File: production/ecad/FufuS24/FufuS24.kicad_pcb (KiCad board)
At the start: 4 copper layers, 120 x 120 mm, 144 parts, among them J1 Conn_01x02, J10 691137710002, J11 USB_B_Micro, J12 691137710002, J13 5033950410, J2 Conn_01x02, J3 691137710002, J5 691137710004, J6 5025840270, J7 691137710002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

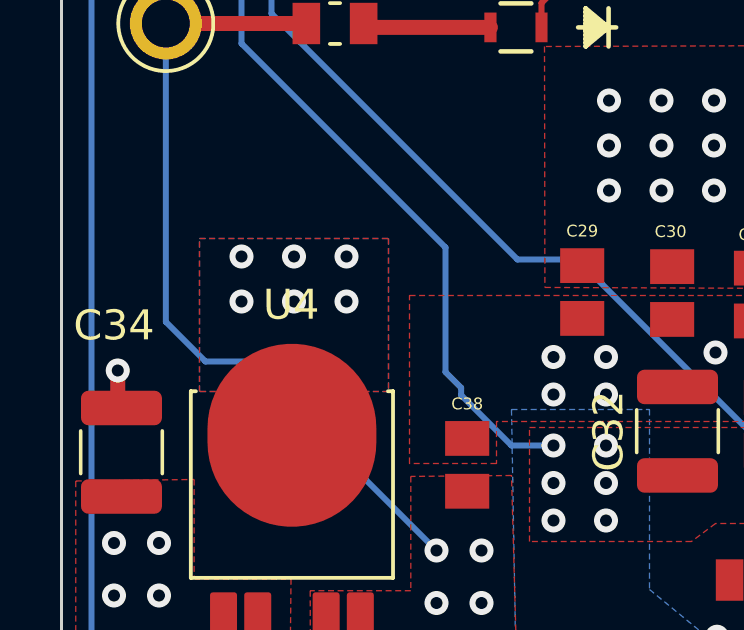
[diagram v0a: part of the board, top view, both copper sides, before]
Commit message: swapped layers
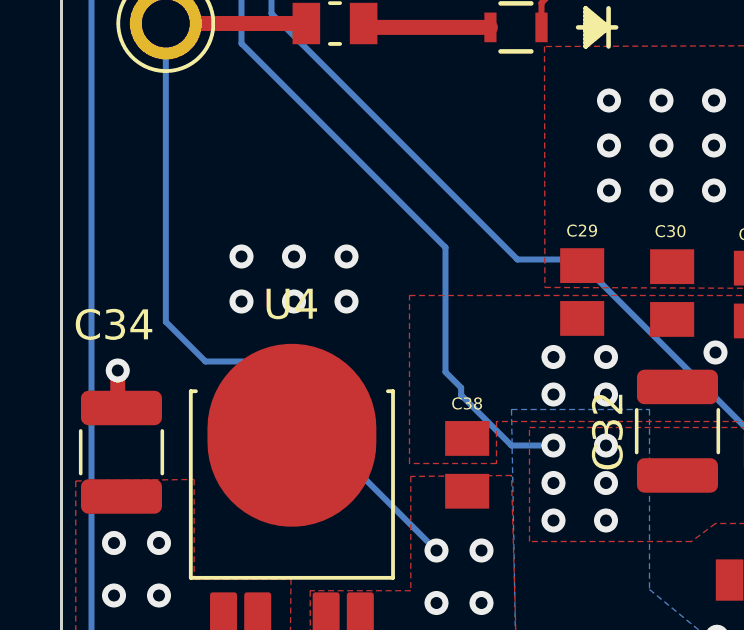
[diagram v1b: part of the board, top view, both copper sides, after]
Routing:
- added copper zone on In2.Cu, net +12V
- added copper zone on In2.Cu, net +3.3V
- added copper zone on In2.Cu, net +48V
- added copper zone on In2.Cu, net +5V
- added copper zone on In1.Cu, net GNDREF
- removed copper zone on In1.Cu, net +12V
- removed copper zone on In1.Cu, net +3.3V
- removed copper zone on In1.Cu, net +48V
- removed copper zone on In1.Cu, net +5V
- removed copper zone on In2.Cu, net GNDREF
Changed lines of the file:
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@@
   (via (at 155.8 127.65) (size 0.8) (drill 0.4) (layers "F.Cu" "B.Cu") (free) (net 10))
   (via (at 137.25 126.4) (size 0.8) (drill 0.4) (layers "F.Cu" "B.Cu") (free) (net 10))
-  (segment (start 176.75 96.5) (end 176.25 96) (width 0.5) (layer "In1.Cu") (net 10))
-  (segment (start 176.25 96) (end 174.2 96) (width 0.5) (layer "In1.Cu") (net 10))
+  (segment (start 176.75 96.5) (end 176.25 96) (width 0.5) (layer "In2.Cu") (net 10))
+  (segment (start 176.25 96) (end 174.2 96) (width 0.5) (layer "In2.Cu") (net 10))
   (segment (start 104.575 85.575) (end 103.5 84.5) (width 0.2) (layer "B.Cu") (net 10))
   (segment (start 136.575 39) (end 140.75 39) (width 0.2) (layer "B.Cu") (net 10))
@@
   (segment (start 184.045 125.295) (end 184.25 125.5) (width 0.1348) (layer "F.Cu") (net 65))
   (segment (start 180.5 125.295) (end 184.045 125.295) (width 0.5) (layer "F.Cu") (net 65))
-  (segment (start 177.46 132.29) (end 184.25 125.5) (width 0.2) (layer "In2.Cu") (net 65))
-  (segment (start 175.06 132.29) (end 177.46 132.29) (width 0.2) (layer "In2.Cu") (net 65))
+  (segment (start 177.46 132.29) (end 184.25 125.5) (width 0.2) (layer "In1.Cu") (net 65))
+  (segment (start 175.06 132.29) (end 177.46 132.29) (width 0.2) (layer "In1.Cu") (net 65))
   (segment (start 120.0702 124.1694) (end 118.2668 125.9728) (width 0.5) (layer "F.Cu") (net 66))
   (segment (start 121.819149 124.1694) (end 120.0702 124.1694) (width 0.5) (layer "F.Cu") (net 66))
@@
     )
   )
-  (zone (net 2) (net_name "GNDREF") (layers "F&B.Cu") (hatch edge 0.5)
+  (zone (net 2) (net_name "GNDREF") (layer "In1.Cu") (hatch edge 0.5)
     (priority 15)
     (connect_pads yes (clearance 0.5))
@@
     )
   )
-  (zone (net 10) (net_name "+5V") (layer "In1.Cu") (hatch edge 0.5)
+  (zone (net 2) (net_name "GNDREF") (layer "In1.Cu") (hatch edge 0.5)
+    (priority 8)
+    (connect_pads yes (clearance 0.5))
+    (min_thickness 0.25) (filled_areas_thickness no)
+    (fill yes (thermal_gap 0.5) (thermal_bridge_width 0.5))
+    (polygon
+      (pts
+        (xy 75.725 23.175)
+        (xy 74.45 156.6)
+        (xy 210.775 157.15)
+        (xy 212.2 23.9)
+      )
+    )
+  )
+  (zone (net 10) (net_name "+5V") (layer "In2.Cu") (hatch edge 0.5)
     (priority 23)
     (connect_pads (clearance 0.5))
@@
     )
   )
-  (zone (net 10) (net_name "+5V") (layer "In1.Cu") (hatch edge 0.5)
+  (zone (net 10) (net_name "+5V") (layer "In2.Cu") (hatch edge 0.5)
     (priority 24)
     (connect_pads (clearance 0.5))
@@
     )
   )
-  (zone (net 10) (net_name "+5V") (layer "In1.Cu") (hatch edge 0.5)
+  (zone (net 10) (net_name "+5V") (layer "In2.Cu") (hatch edge 0.5)
     (priority 25)
     (connect_pads (clearance 0.5))
@@
     )
   )
-  (zone (net 10) (net_name "+5V") (layer "In1.Cu") (hatch edge 0.5)
+  (zone (net 10) (net_name "+5V") (layer "In2.Cu") (hatch edge 0.5)
     (priority 5)
     (connect_pads (clearance 0.5))
@@
     )
   )
-  (zone (net 10) (net_name "+5V") (layer "In1.Cu") (hatch edge 0.5)
+  (zone (net 10) (net_name "+5V") (layer "In2.Cu") (hatch edge 0.5)
     (priority 28)
     (connect_pads (clearance 0.5))
@@
     )
   )
-  (zone (net 1) (net_name "+48V") (layer "In1.Cu") (hatch edge 0.5)
+  (zone (net 1) (net_name "+48V") (layer "In2.Cu") (hatch edge 0.5)
     (priority 27)
     (connect_pads (clearance 0.5))
@@
     )
   )
-  (zone (net 15) (net_name "+12V") (layer "In1.Cu") (hatch edge 0.5)
+  (zone (net 15) (net_name "+12V") (layer "In2.Cu") (hatch edge 0.5)
     (priority 33)
     (connect_pads (clearance 0.5))
@@
     )
   )
-  (zone (net 1) (net_name "+48V") (layer "In1.Cu") (hatch edge 0.5)
+  (zone (net 1) (net_name "+48V") (layer "In2.Cu") (hatch edge 0.5)
     (priority 2)
     (connect_pads (clearance 0.5))
@@
     )
   )
-  (zone (net 15) (net_name "+12V") (layer "In1.Cu") (hatch edge 0.5)
+  (zone (net 15) (net_name "+12V") (layer "In2.Cu") (hatch edge 0.5)
     (priority 34)
     (connect_pads (clearance 0.45))
@@
     )
   )
-  (zone (net 19) (net_name "+3.3V") (layer "In1.Cu") (hatch edge 0.5)
+  (zone (net 19) (net_name "+3.3V") (layer "In2.Cu") (hatch edge 0.5)
     (priority 22)
     (connect_pads (clearance 0.5))
@@
       )
     )
-  )
-  (zone (net 2) (net_name "GNDREF") (layer "In2.Cu") (hatch edge 0.5)
-    (priority 8)
-    (connect_pads yes (clearance 0.5))
-    (min_thickness 0.25) (filled_areas_thickness no)
-    (fill yes (thermal_gap 0.5) (thermal_bridge_width 0.5))
-    (polygon
-      (pts
-        (xy 75.725 23.175)
-        (xy 74.45 156.6)
-        (xy 210.775 157.15)
-        (xy 212.2 23.9)
-      )
-    )

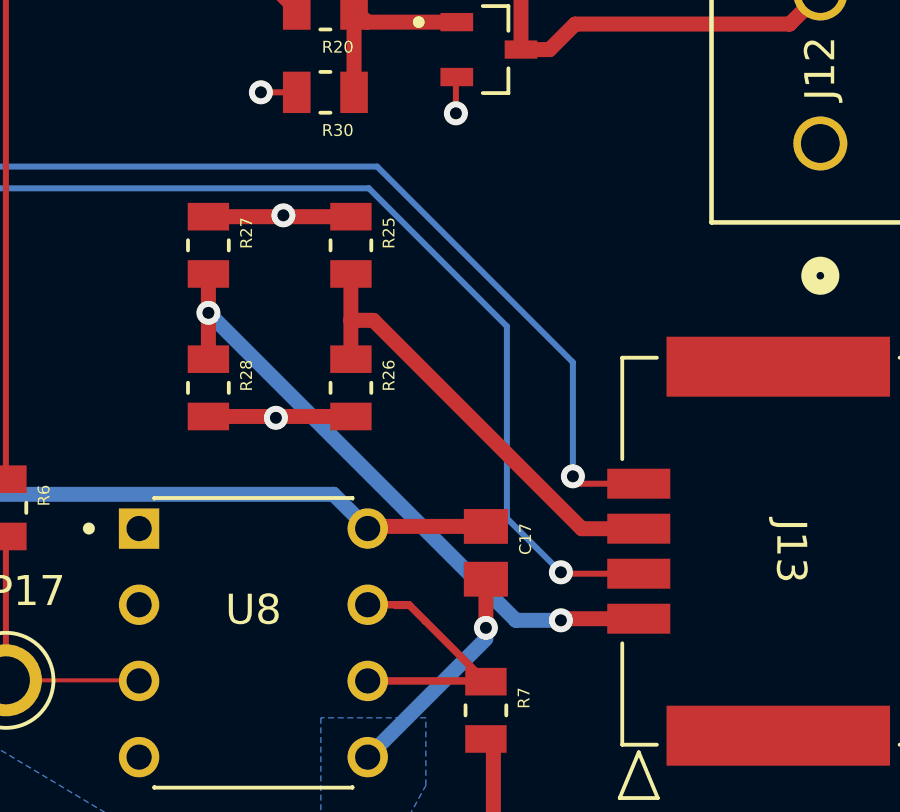
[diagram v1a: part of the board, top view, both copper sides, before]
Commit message: updated water sensor
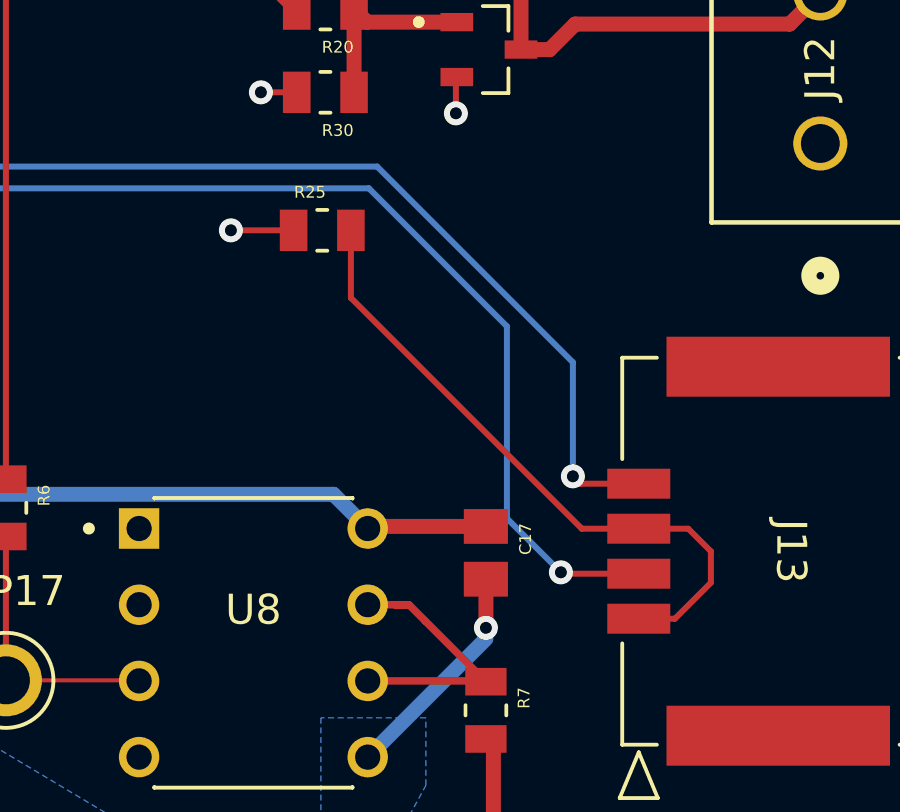
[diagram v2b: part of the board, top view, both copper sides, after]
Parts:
- removed R26, R27, R28: 10k, footprints:RESC2012X60N
- moved R25 1.08 mm to (178.0, 97.0), turned to 0 degrees
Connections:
- J13 pad 1: /Water Dispensing/Watersense_Mode_2 -> Net-(J13-Pad1)
- J13 pad 3: /Water Dispensing/Watersense_Mode_1 -> Net-(J13-Pad1)
- R25 pad 2: /Water Dispensing/Watersense_Mode_1 -> Net-(J13-Pad1)
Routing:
- net Net-(J13-Pad1): track 0.00 -> 21.7 mm
- net /Water Dispensing/Watersense_Mode_2: track 21.5 -> 0.00 mm, vias 2 -> 0
- net /Water Dispensing/Watersense_Mode_1: track 15.3 -> 0.00 mm
- net +5V: track 53.4 -> 48.0 mm
- net GNDREF: track 71.5 -> 66.7 mm, vias 93 -> 92

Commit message: updated layout
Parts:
- removed D10, D11: 150080GS75000, footprints:LED_GS75000_WRE
- removed R44, R45, R46: R_US, footprints:RESC2012X60N
- removed TP6, TP7, TP8: 5014, footprints:TP_5014
- removed U12: Pololu_DRV8711_Motor_Driver, footprints:POLOLU_36v4
- added C40: 100n, footprints:WCAP-CSGP_885012206026, F.Cu at (155.6, 50.3)
- added C41: 100n, footprints:WCAP-CSGP_885012206026, F.Cu at (162.0, 50.6)
- added J17: Conn_01x14_Socket, Connector_PinSocket_2.54mm:PinSocket_1x14_P2.54mm_Vertical, F.Cu at (194.9, 48.0)
- added R26: TBD, footprints:RESC2012X60N, F.Cu at (153.8, 50.4)
- added U3: TXS0101DBVR, footprints:LevelShifter_Motor, F.Cu at (158.8, 51.0)
- moved J2 54.2 mm to (156.2, 38.7), turned to 0 degrees
- moved R1 48.7 mm to (156.2, 42.6), turned to -90 degrees
- moved TP19 9.52 mm to (187.3, 44.8)
- moved J12 1.80 mm to (194.5, 95.9)
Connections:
- J5 pad 1: Net-(U12-BOUT2) -> GNDREF
- J5 pad 2: Net-(U12-BOUT1) -> unconnected-(J5-Pad2)
- J5 pad 3: Net-(U12-AOUT2) -> unconnected-(J5-Pad3)
- U1 pad 2: unconnected-(U1-GPIO0-Pad2) -> GPIO_0
- U1 pad 27: Motor_SLP -> GPIO_7
- U1 pad 28: Motor_RST -> GPIO_8
- U1 pad 3: unconnected-(U1-GPIO1-Pad3) -> GPIO_1
- U1 pad 30: unconnected-(U1-GPIO19-Pad30) -> GPIO_19
- U1 pad 36: Motor_SPI1_RX -> GPIO_24
- U1 pad 37: Motor_SPI1_CSn -> GPIO_25
- U1 pad 38: Motor_SPI1_CLK -> GPIO_26
- U1 pad 39: Motor_SPI1_TX -> GPIO_27
- U1 pad 5: unconnected-(U1-GPIO3-Pad5) -> GPIO_3
- U1 pad 6: Motor_BIN1 -> Motor_PWM
- U1 pad 7: Motor_BIN2 -> GPIO_4
- U1 pad 8: Motor_Step -> GPIO_5
- U1 pad 9: Motor_DIR -> GPIO_6
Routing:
- net Motor_RST: track 82.7 -> 0.00 mm, vias 1 -> 0
- net GPIO_5: track 0.00 -> 82.6 mm, vias 0 -> 1
- net GPIO_6: track 0.00 -> 82.3 mm, vias 0 -> 1
- net GPIO_4: track 0.00 -> 82.3 mm, vias 0 -> 1
- net GPIO_8: track 0.00 -> 81.9 mm, vias 0 -> 1
- net GPIO_7: track 0.00 -> 81.9 mm, vias 0 -> 1
- net GPIO_19: track 0.00 -> 81.4 mm, vias 0 -> 1
- net GPIO_3: track 0.00 -> 81.2 mm, vias 0 -> 1
- net GPIO_1: track 0.00 -> 81.1 mm, vias 0 -> 1
- net GPIO_0: track 0.00 -> 80.8 mm, vias 0 -> 1
- net GPIO_27: track 0.00 -> 80.2 mm, vias 0 -> 1
- net GPIO_26: track 0.00 -> 79.1 mm, vias 0 -> 1
- net GPIO_25: track 0.00 -> 78.1 mm, vias 0 -> 1
- net GPIO_24: track 0.00 -> 77.4 mm, vias 0 -> 1
- net Motor_SLP: track 76.6 -> 0.00 mm, vias 1 -> 0
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- removed copper zone on In2.Cu, net +12V
- removed copper zone on B.Cu, net +5V

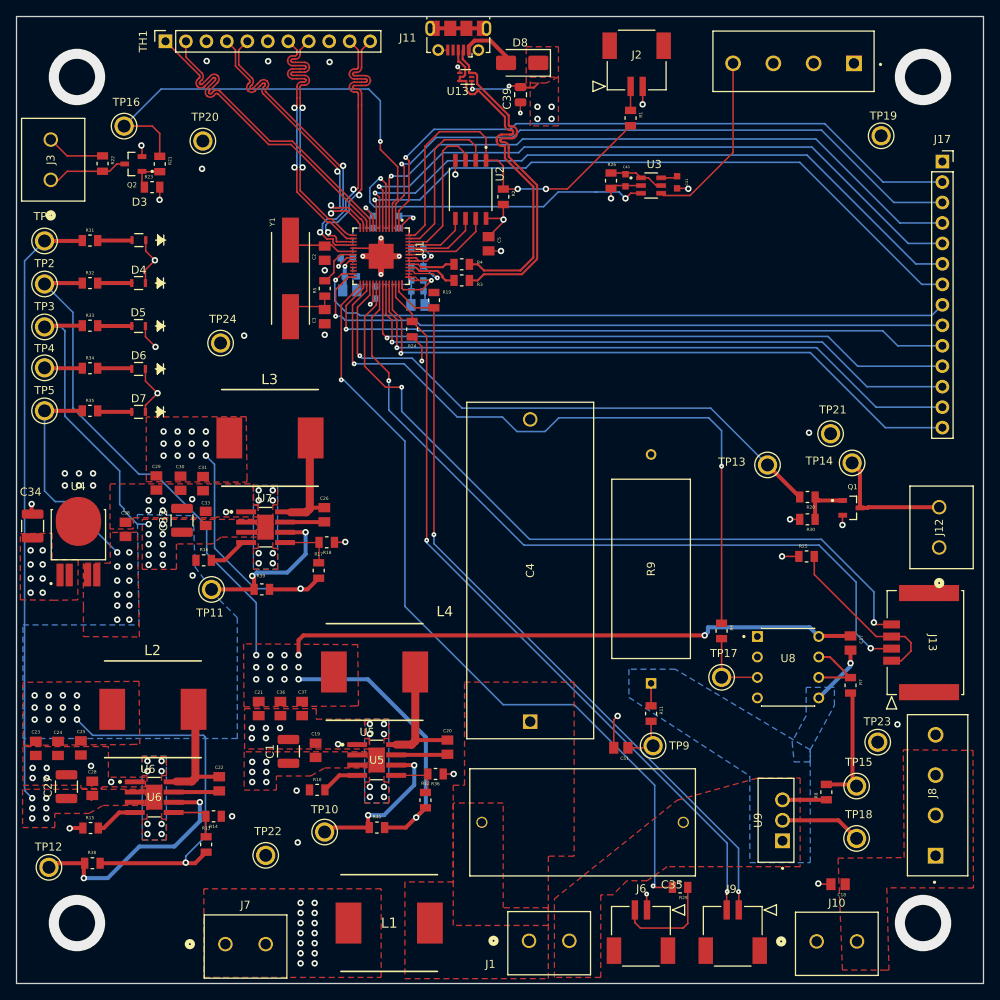
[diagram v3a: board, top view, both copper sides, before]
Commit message: updated power planes
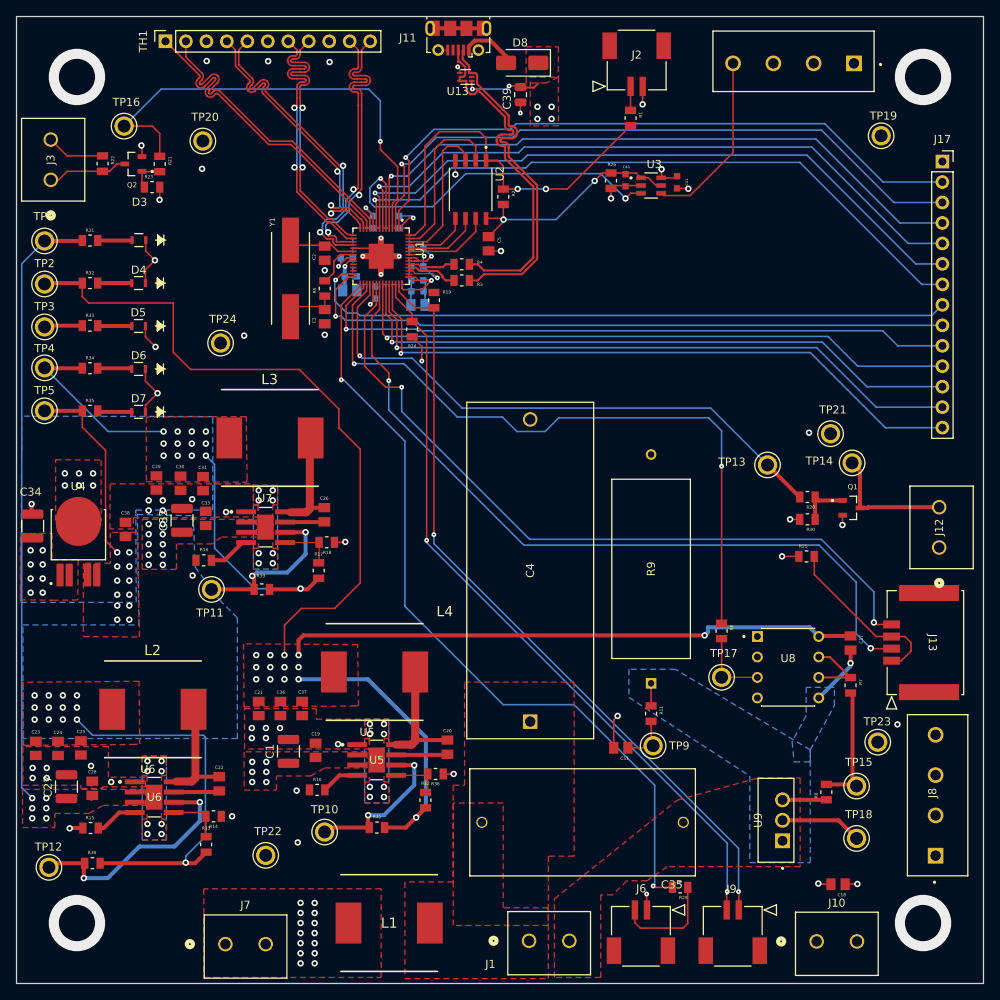
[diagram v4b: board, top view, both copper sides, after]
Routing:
- net +12V: track 91.2 -> 59.4 mm
- net +16V: track 169.4 -> 192.2 mm
- net +5V: track 50.0 -> 70.7 mm, vias 28 -> 30
- net +3.3V: track 83.2 -> 96.2 mm, vias 20 -> 21
- net Motor_PWM: track 45.6 -> 47.2 mm
- added copper zone on In2.Cu, net +12V
- added copper zone on B.Cu, net +5V

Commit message: fixed some DRC
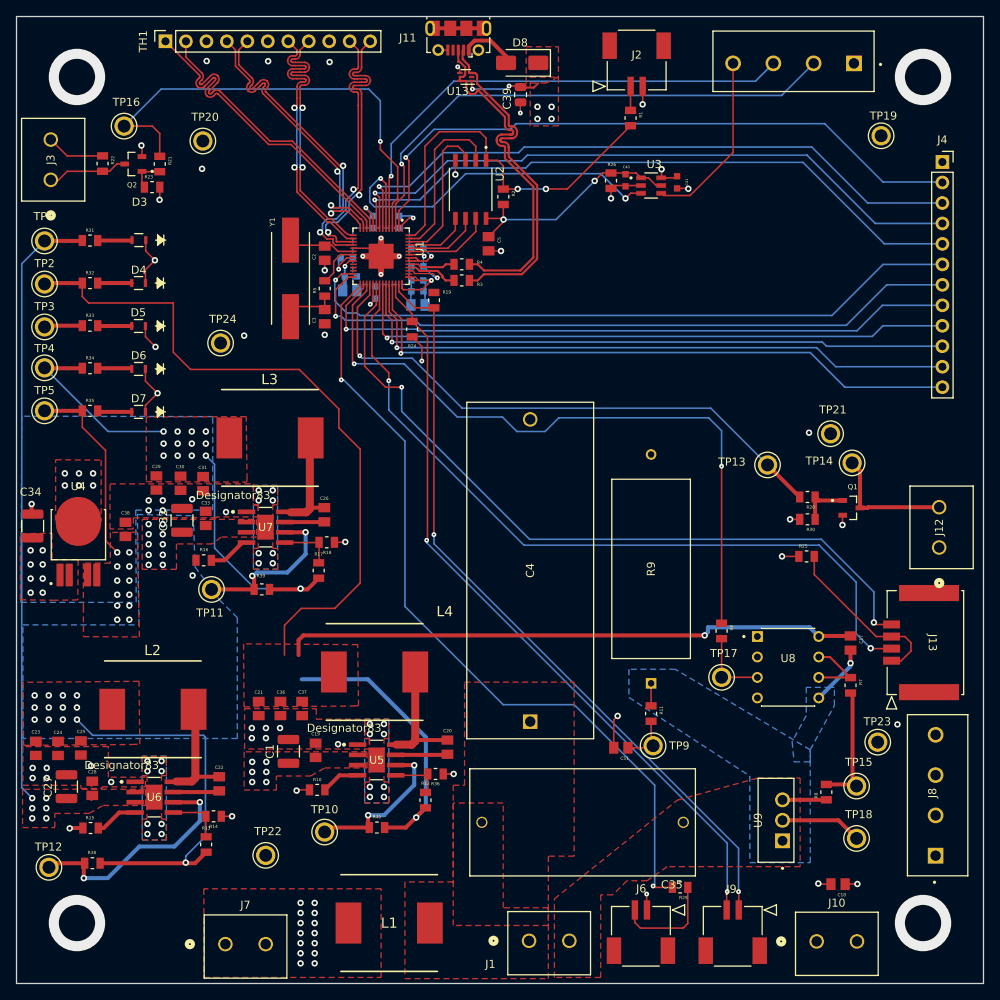
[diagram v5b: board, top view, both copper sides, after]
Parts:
- removed J17: Conn_01x14_Socket, Connector_PinSocket_2.54mm:PinSocket_1x14_P2.54mm_Vertical
- added J4: Conn_01x12_Socket, Connector_PinSocket_2.54mm:PinSocket_1x12_P2.54mm_Vertical, F.Cu at (194.9, 48.1)
- U5, U6, U7: footprint footprints:DDA0008E-IPC_A -> footprints:DDA0008E-IPC_B
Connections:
- J5 pad 2: unconnected-(J5-Pad2) -> Motor_Enable
- J5 pad 3: unconnected-(J5-Pad3) -> Motor_Direction
- U1 pad 3: GPIO_1 -> Motor_Enable
- U1 pad 5: GPIO_3 -> Motor_Direction
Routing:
- net GPIO_3: track 81.2 -> 0.00 mm, vias 1 -> 0
- net GPIO_1: track 81.1 -> 0.00 mm, vias 1 -> 0
- net Motor_Enable: track 0.00 -> 65.8 mm, vias 0 -> 1
- net Motor_Direction: track 0.00 -> 62.2 mm, vias 0 -> 1
- net GNDREF: track 73.9 -> 77.7 mm, vias 90 -> 89
- net GPIO_8: track 81.9 -> 84.0 mm
- net GPIO_26: track 79.1 -> 77.0 mm
- net GPIO_7: track 81.9 -> 83.9 mm
- net GPIO_6: track 82.3 -> 80.2 mm
- net GPIO_5: track 82.6 -> 80.5 mm
- net GPIO_4: track 82.3 -> 80.2 mm
- net GPIO_27: track 80.2 -> 78.2 mm
- net GPIO_25: track 78.1 -> 76.0 mm
- net GPIO_24: track 77.4 -> 76.5 mm
- net +3.3V: track 96.2 -> 96.9 mm
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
